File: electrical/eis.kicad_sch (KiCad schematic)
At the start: 7 parts

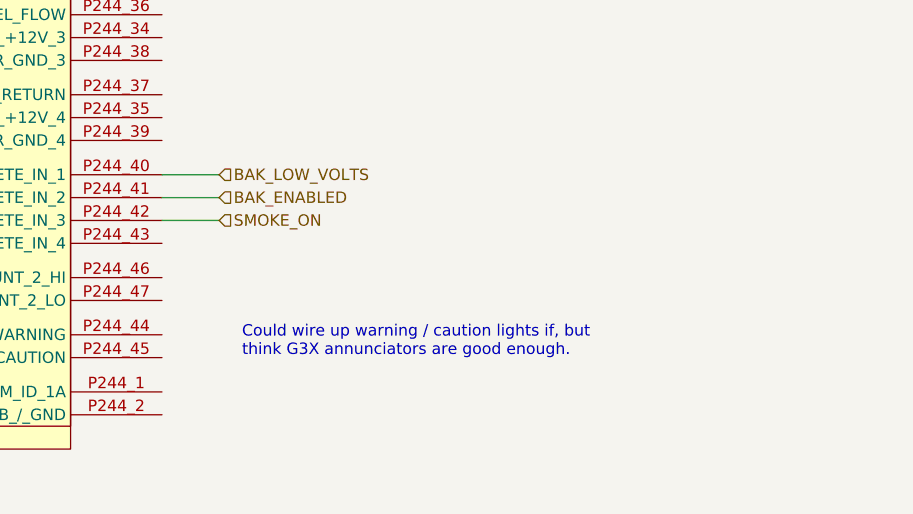
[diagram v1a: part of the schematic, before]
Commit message: Added Warning/Caution lights/buttons. Moved smoke on to GAD 27. Added glide button to GAD 27. Added lighting switched pots to GEA 24.
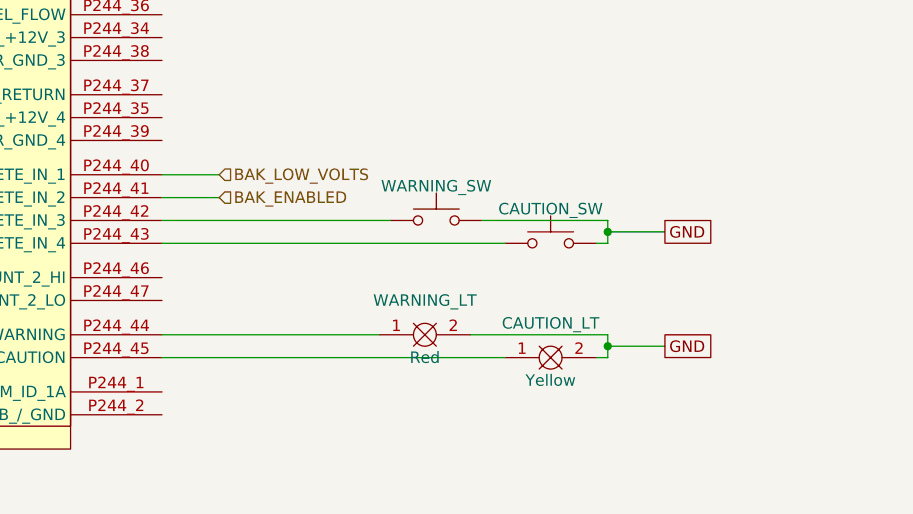
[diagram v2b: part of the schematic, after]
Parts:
- added CAUTION_LT: Yellow, symbol FlyerX:Bulb
- added CAUTION_SW, WARNING_SW: SW_Push, symbol Switch:SW_Push
- added WARNING_LT: Red, symbol FlyerX:Bulb
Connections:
- net GND: now also CAUTION_LT.2, CAUTION_SW.2, WARNING_LT.2, WARNING_SW.2
- net at GEA24.P244_43 (DISCRETE_IN_4): now also CAUTION_SW.1
- net at GEA24.P244_44 (DISCRETE_OUT_1/WARNING): now also WARNING_LT.1
- net at GEA24.P244_45 (DISCRETE_OUT_2/CAUTION): now also CAUTION_LT.1
- net SMOKE_ON: no longer names the net of GEA24.P244_42 (DISCRETE_IN_3)
- net SMOKE_ON: now also WARNING_SW.1
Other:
- note removed: "Could wire up warning / caution lights if, but think G3X annunciators are good enough."
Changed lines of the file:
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@@
   (junction (at 95.25 33.02) (diameter 0) (color 0 0 0 0)
   )
+  (junction (at 116.84 340.36) (diameter 0) (color 0 0 0 0)
+  )
   (junction (at 69.85 184.15) (diameter 0) (color 0 0 0 0)
   )
   (junction (at 69.85 190.5) (diameter 0) (color 0 0 0 0)
+  )
+  (junction (at 116.84 353.06) (diameter 0) (color 0 0 0 0)
   )
   (no_connect (at 137.16 196.85))
@@
     (stroke (width 0) (type default))
   )
+  (wire (pts (xy 116.84 341.63) (xy 116.84 340.36))
+    (stroke (width 0) (type default))
+  )
   (wire (pts (xy 67.31 312.42) (xy 73.66 312.42))
     (stroke (width 0) (type default))
@@
     (stroke (width 0) (type default))
   )
+  (wire (pts (xy 116.84 353.06) (xy 123.19 353.06))
+    (stroke (width 0) (type default))
+  )
+  (wire (pts (xy 116.84 351.79) (xy 116.84 353.06))
+    (stroke (width 0) (type default))
+  )
   (wire (pts (xy 67.31 233.68) (xy 96.52 233.68))
     (stroke (width 0) (type default))
@@
     (stroke (width 0) (type default))
   )
+  (wire (pts (xy 102.87 339.09) (xy 116.84 339.09))
+    (stroke (width 0) (type default))
+  )
   (wire (pts (xy 67.31 190.5) (xy 69.85 190.5))
     (stroke (width 0) (type default))
@@
     (stroke (width 0) (type default))
   )
-  (wire (pts (xy 67.31 339.09) (xy 73.66 339.09))
-    (stroke (width 0) (type default))
-  )
   (wire (pts (xy 67.31 278.13) (xy 85.09 278.13))
     (stroke (width 0) (type default))
@@
     (stroke (width 0) (type default))
   )
+  (wire (pts (xy 116.84 340.36) (xy 123.19 340.36))
+    (stroke (width 0) (type default))
+  )
   (wire (pts (xy 90.17 121.92) (xy 92.71 121.92))
     (stroke (width 0) (type default))
@@
     (stroke (width 0) (type default))
   )
+  (wire (pts (xy 67.31 339.09) (xy 92.71 339.09))
+    (stroke (width 0) (type default))
+  )
   (wire (pts (xy 67.31 36.83) (xy 73.66 36.83))
     (stroke (width 0) (type default))
@@
     (stroke (width 0) (type default))
   )
+  (wire (pts (xy 67.31 351.79) (xy 91.44 351.79))
+    (stroke (width 0) (type default))
+  )
   (wire (pts (xy 67.31 240.03) (xy 109.22 240.03))
     (stroke (width 0) (type default))
@@
     (stroke (width 0) (type default))
   )
+  (wire (pts (xy 101.6 351.79) (xy 116.84 351.79))
+    (stroke (width 0) (type default))
+  )
+  (wire (pts (xy 116.84 339.09) (xy 116.84 340.36))
+    (stroke (width 0) (type default))
+  )
+  (wire (pts (xy 115.57 354.33) (xy 116.84 354.33))
+    (stroke (width 0) (type default))
+  )
   (wire (pts (xy 67.31 287.02) (xy 85.09 287.02))
     (stroke (width 0) (type default))
@@
     (stroke (width 0) (type default))
   )
+  (wire (pts (xy 67.31 354.33) (xy 105.41 354.33))
+    (stroke (width 0) (type default))
+  )
+  (wire (pts (xy 115.57 341.63) (xy 116.84 341.63))
+    (stroke (width 0) (type default))
+  )
   (wire (pts (xy 67.31 184.15) (xy 69.85 184.15))
     (stroke (width 0) (type default))
@@
     (stroke (width 0) (type default))
   )
+  (wire (pts (xy 116.84 354.33) (xy 116.84 353.06))
+    (stroke (width 0) (type default))
+  )
   (wire (pts (xy 106.68 236.22) (xy 113.03 236.22))
     (stroke (width 0) (type default))
@@
   )
   (wire (pts (xy 96.52 227.33) (xy 102.87 227.33))
+    (stroke (width 0) (type default))
+  )
+  (wire (pts (xy 67.31 341.63) (xy 105.41 341.63))
     (stroke (width 0) (type default))
   )
@@
     (effects (font (size 1.27 1.27)) (justify left bottom))
   )
-  (text "Could wire up warning / caution lights if, but\nthink G3X annunciators are good enough."
-    (at 76.2 354.33 0)
-    (effects (font (size 1.27 1.27)) (justify left bottom))
-  )
   (text "Maybe connect RS-232 like CO Detector\nTry to P241_4\nPage 24-26"
     (at 135.89 204.47 0)
@@
     )
   )
+  (global_label "GND" (shape passive) (at 123.19 340.36 0) (fields_autoplaced)
+    (effects (font (size 1.27 1.27)) (justify left))
+    (property "Intersheetrefs" "${INTERSHEET_REFS}" (at 128.9344 340.36 0)
+      (effects (font (size 1.27 1.27)) (justify left) hide)
+    )
+  )
+  (global_label "GND" (shape passive) (at 123.19 353.06 0) (fields_autoplaced)
+    (effects (font (size 1.27 1.27)) (justify left))
+    (property "Intersheetrefs" "${INTERSHEET_REFS}" (at 128.9344 353.06 0)
+      (effects (font (size 1.27 1.27)) (justify left) hide)
+    )
+  )
   (hierarchical_label "EIS_SERIAL_GND" (shape passive) (at 73.66 41.91 0) (fields_autoplaced)
     (effects (font (size 1.27 1.27)) (justify left))
@@
   )
   (hierarchical_label "EIS_SERIAL_IN" (shape input) (at 73.66 39.37 0) (fields_autoplaced)
-    (effects (font (size 1.27 1.27)) (justify left))
-  )
-  (hierarchical_label "SMOKE_ON" (shape input) (at 73.66 339.09 0) (fields_autoplaced)
     (effects (font (size 1.27 1.27)) (justify left))
   )
@@
   (hierarchical_label "BAK_LOW_VOLTS" (shape input) (at 73.66 334.01 0) (fields_autoplaced)
     (effects (font (size 1.27 1.27)) (justify left))
+  )
+  (symbol (lib_id "Switch:SW_Push") (at 97.79 339.09 0) (unit 1)
+    (in_bom yes) (on_board yes) (dnp no)
+    (property "Reference" "WARNING_SW" (at 97.79 335.28 0)
+      (effects (font (size 1.27 1.27)))
+    )
+    (property "Value" "SW_Push" (at 97.79 334.01 0)
+      (effects (font (size 1.27 1.27)) hide)
+    )
+    (property "Footprint" "" (at 97.79 334.01 0)
+      (effects (font (size 1.27 1.27)) hide)
+    )
+    (property "Datasheet" "~" (at 97.79 334.01 0)
+      (effects (font (size 1.27 1.27)) hide)
+    )
+    (pin "1")
+    (pin "2")
+    (instances
+      (project "electrical"
+        (path "/e8ec215a-dbe2-4eba-a577-e50a0a128049/72184f52-5cc1-469a-bd6f-4bd63aea59bf"
+          (reference "WARNING_SW") (unit 1)
+        )
+      )
+    )
   )
   (symbol (lib_id "flyerx:Kavlico_P4055") (at 100.33 115.57 0) (mirror y) (unit 1)
@@
     )
   )
+  (symbol (lib_id "FlyerX:Bulb") (at 109.22 353.06 0) (unit 1)
+    (in_bom yes) (on_board yes) (dnp no)
+    (property "Reference" "CAUTION_LT" (at 110.49 350.52 0)
+      (effects (font (size 1.27 1.27)))
+    )
+    (property "Value" "Yellow" (at 110.49 356.87 0)
+      (effects (font (size 1.27 1.27)))
+    )
+    (property "Footprint" "" (at 110.49 351.79 0)
+      (effects (font (size 1.27 1.27)) hide)
+    )
+    (property "Datasheet" "" (at 110.49 351.79 0)
+      (effects (font (size 1.27 1.27)) hide)
+    )
+    (pin "1")
+    (pin "2")
+    (instances
+      (project "electrical"
+        (path "/e8ec215a-dbe2-4eba-a577-e50a0a128049/72184f52-5cc1-469a-bd6f-4bd63aea59bf"
+          (reference "CAUTION_LT") (unit 1)
+        )
+      )
+    )
+  )
   (symbol (lib_id "flyerx:Ray_Allen_POS-12") (at 99.06 274.32 0) (mirror y) (unit 1)
     (in_bom yes) (on_board yes) (dnp no)
@@
         )
       )
+    )
+  )
+  (symbol (lib_id "Switch:SW_Push") (at 110.49 341.63 0) (unit 1)
+    (in_bom yes) (on_board yes) (dnp no)
+    (property "Reference" "CAUTION_SW" (at 110.49 337.82 0)
+      (effects (font (size 1.27 1.27)))
+    )
+    (property "Value" "SW_Push" (at 110.49 336.55 0)
+      (effects (font (size 1.27 1.27)) hide)
+    )
+    (property "Footprint" "" (at 110.49 336.55 0)
+      (effects (font (size 1.27 1.27)) hide)
+    )
+    (property "Datasheet" "~" (at 110.49 336.55 0)
+      (effects (font (size 1.27 1.27)) hide)
+    )
+    (pin "1")
+    (pin "2")
+    (instances
+      (project "electrical"
+        (path "/e8ec215a-dbe2-4eba-a577-e50a0a128049/72184f52-5cc1-469a-bd6f-4bd63aea59bf"
+          (reference "CAUTION_SW") (unit 1)
+        )
+      )
+    )
+  )
+  (symbol (lib_id "FlyerX:Bulb") (at 95.25 350.52 0) (unit 1)
+    (in_bom yes) (on_board yes) (dnp no)
+    (property "Reference" "WARNING_LT" (at 96.52 347.98 0)
+      (effects (font (size 1.27 1.27)))
+    )
+    (property "Value" "Red" (at 96.52 354.33 0)
+      (effects (font (size 1.27 1.27)))
+    )
+    (property "Footprint" "" (at 96.52 349.25 0)
+      (effects (font (size 1.27 1.27)) hide)
+    )
+    (property "Datasheet" "" (at 96.52 349.25 0)
+      (effects (font (size 1.27 1.27)) hide)
+    )
+    (pin "1")
+    (pin "2")
+    (instances
+      (project "electrical"
+        (path "/e8ec215a-dbe2-4eba-a577-e50a0a128049/72184f52-5cc1-469a-bd6f-4bd63aea59bf"
+          (reference "WARNING_LT") (unit 1)
+        )
+      )

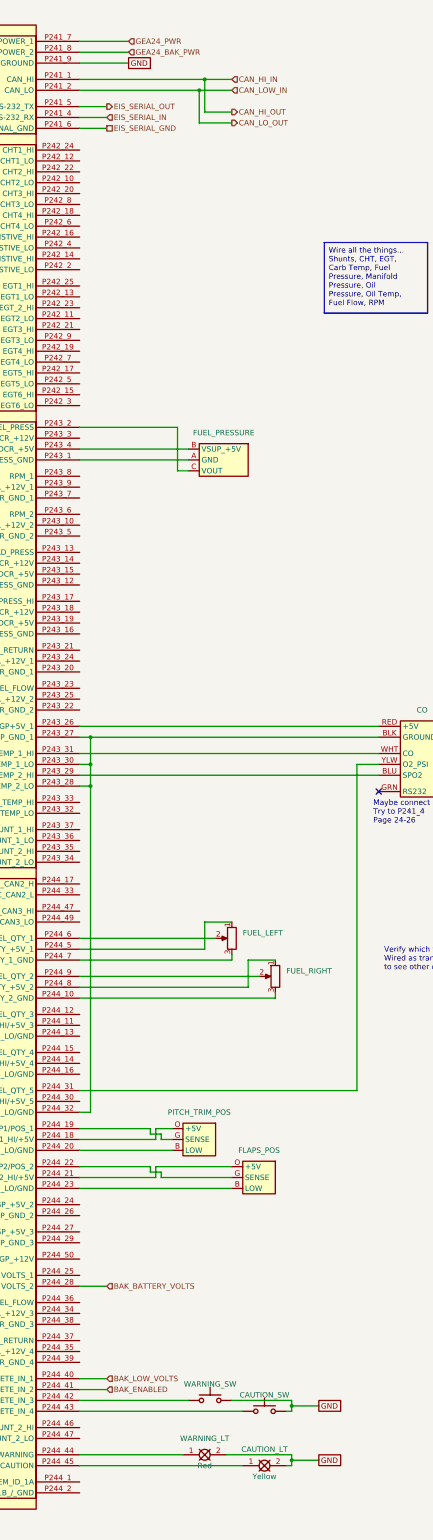
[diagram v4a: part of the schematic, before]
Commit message: Updated electrical to not use IBBS. Also, added BT adapter and 3P3T switch.
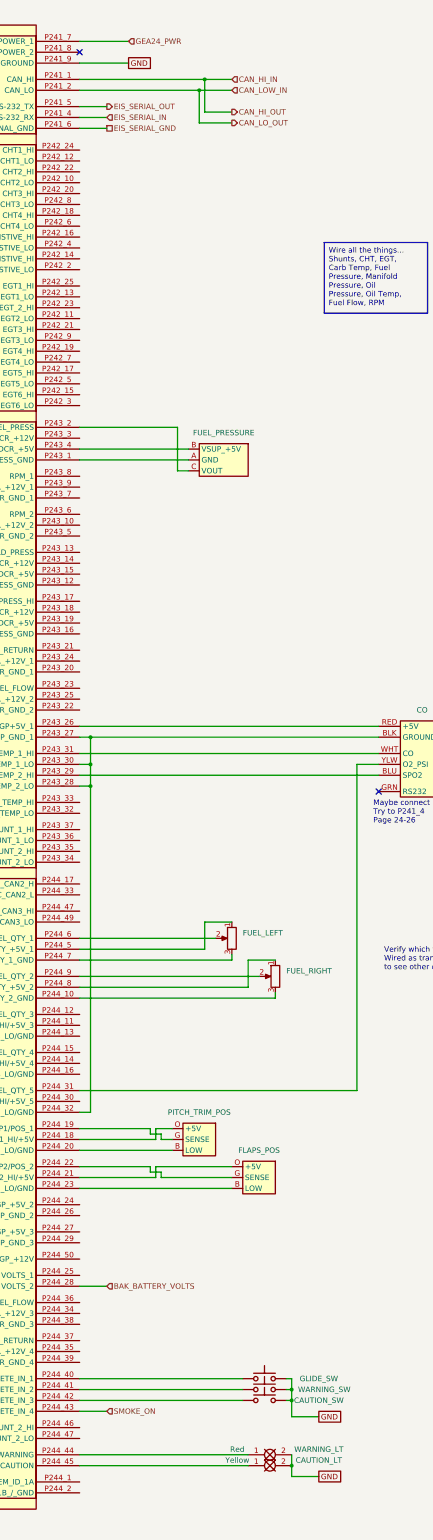
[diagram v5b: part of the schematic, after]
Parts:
- added GLIDE_SW: SW_Push, symbol Switch:SW_Push
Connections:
- net BAK_ENABLED is gone; now on an unnamed net: GEA24.P244_41 (DISCRETE_IN_2)
- net GND: now also GLIDE_SW.2
- net at WARNING_SW.1: no longer GEA24.P244_42 (DISCRETE_IN_3)
- net at CAUTION_SW.1: now also GEA24.P244_42 (DISCRETE_IN_3); no longer GEA24.P244_43 (DISCRETE_IN_4)
- net BAK_LOW_VOLTS: no longer names the net of GEA24.P244_40 (DISCRETE_IN_1)
- net BAK_LOW_VOLTS: now also GLIDE_SW.1
- net GEA24_BAK_PWR: no longer names the net of GEA24.P241_8 (AIRCRAFT_POWER_2)
- new net SMOKE_ON: GEA24.P244_43 (DISCRETE_IN_4)
- no-connect marks 1 -> 2
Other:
- moved on the sheet: CAUTION_LT, CAUTION_SW, WARNING_LT, WARNING_SW
